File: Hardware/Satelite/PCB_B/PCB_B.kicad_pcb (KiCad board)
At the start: 2 copper layers, 54 x 54 mm, 66 parts, among them IC1 MCP1642B-50I_MS, IC2 MCP1642B-50I_MS, J1 Conector_PCB_B-C, J2 Conector_PCB_A-B, U1 MIC5323-3.3YD5_TR, U2 ADP2108AUJ-3.3, U3 INA194, U4 MCP6001-OT, U5 INA194, U6 MCP6001-OT, U7 INA194, U8 BQ24091DGQT, U9 BQ27441DRZR-G1A

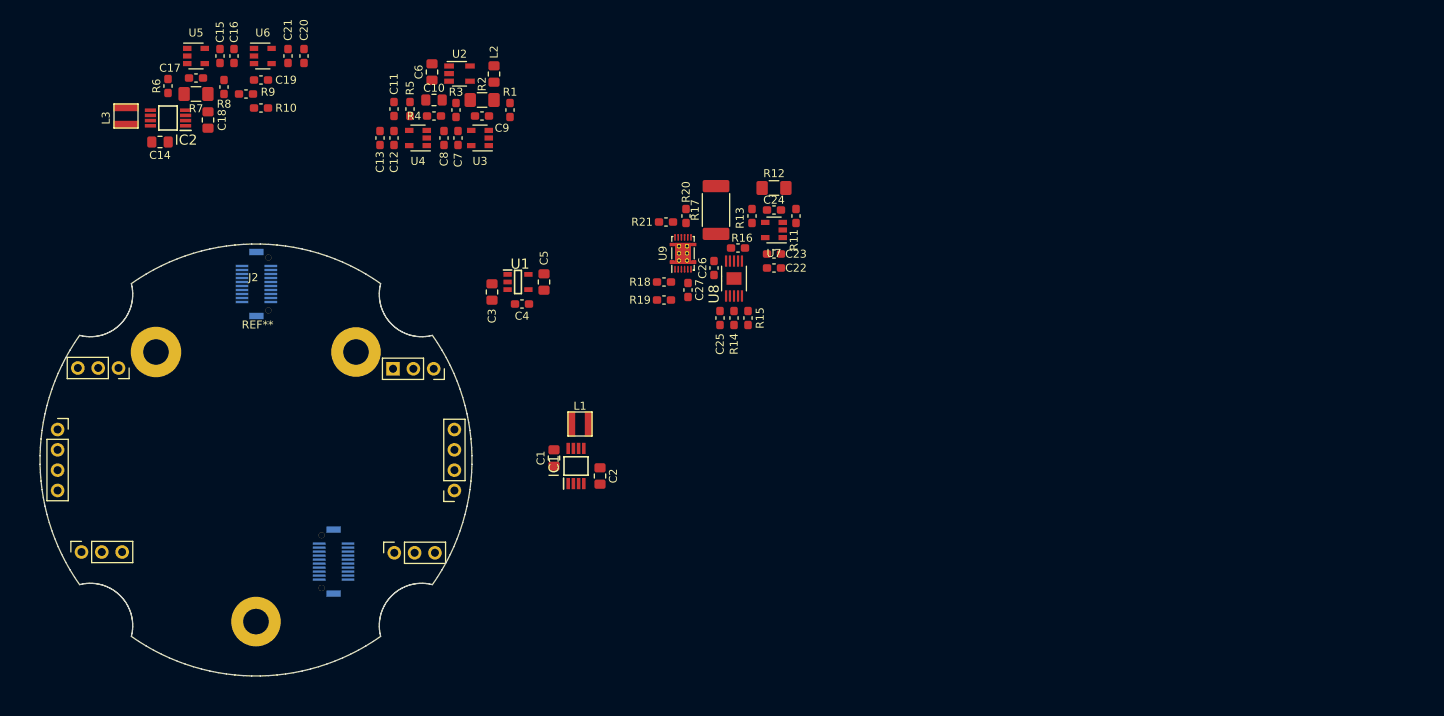
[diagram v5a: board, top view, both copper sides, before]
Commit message: Modifificaciones de pines en conector PCB_B-C
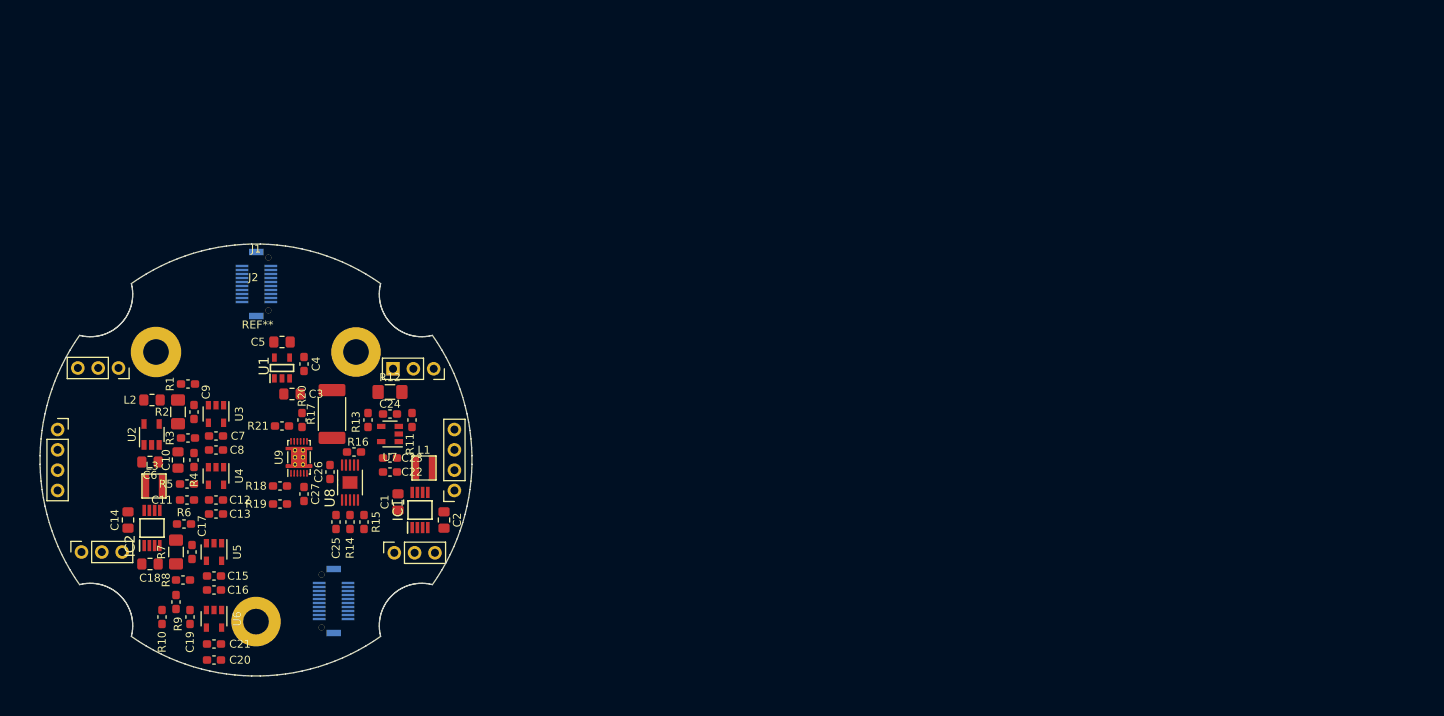
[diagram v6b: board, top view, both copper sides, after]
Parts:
- moved C20 76.3 mm to (-5.25, 25.0), turned to 0 degrees
- moved C21 74.1 mm to (-5.25, 23.0), turned to 0 degrees
- moved U6 70.6 mm to (-5.25, 19.9), turned to 270 degrees
- moved C19 67.7 mm to (-8.25, 19.6), turned to 90 degrees
- moved C16 66.8 mm to (-5.25, 16.2), turned to 0 degrees
- moved C15 65.0 mm to (-5.25, 14.5), turned to 0 degrees
- moved R10 64.8 mm to (-11.8, 19.6), turned to 90 degrees
- moved R9 64.1 mm to (-10.0, 17.8), turned to 90 degrees
- moved U5 62.0 mm to (-5.25, 11.5), turned to 270 degrees
- moved R8 61.8 mm to (-9.12, 15.0), turned to 0 degrees
- moved C6 60.2 mm to (-13.2, 0.25), turned to 180 degrees
- moved U2 59.3 mm to (-13.1, -3.19), turned to 90 degrees
- moved C17 59.3 mm to (-8.00, 11.5), turned to 90 degrees
- moved L2 59.1 mm to (-13.0, -7.50), turned to 0 degrees
- moved R7 57.3 mm to (-10.0, 11.5), turned to 90 degrees
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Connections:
- IC2 pad 1: /Power 5V/CTRL -> /ENABLE_5V
- J1 pad 1: +BATT -> GND
- J1 pad 10: /I_SENSE_3V3 -> +3V3_Internal
- J1 pad 11: /V_SENSE_3V3 -> /V_SENSE_5V
- J1 pad 12: /V_SENSE_5V -> /I_SENSE_5V
- J1 pad 13: GND -> +5V
- J1 pad 14: +5V -> /ENABLE_5V
- J1 pad 15: GND -> /V_SENSE_3V3
- J1 pad 16: GND -> /I_SENSE_3V3
- J1 pad 17: GND -> +3V3
- J1 pad 18: +3V3 -> /ENABLE_3V3
- J1 pad 19: +BATT -> /P1
- J1 pad 2: +BATT -> GND
- J1 pad 20: +BATT -> /GPS_TX
- J1 pad 21: /I_SENSE_BATT -> GND
- J1 pad 22: /GPS_TX -> GND
- J1 pad 23: /P1 -> GND
- J1 pad 24: /SCLK -> /GPOUT
- J1 pad 25: /CS -> /SCL
- J1 pad 26: /SDI -> /SDA
- J1 pad 28: /S_PARACAIDAS -> /CHG_DISABLE
- J1 pad 29: /S_GLOBO -> /CHG
- J1 pad 3: +3V3 -> GND
- J1 pad 30: /GPOUT -> /ISET
- J1 pad 31: /SDA -> /I_SENSE_BATT
- J1 pad 32: /SCL -> /S_GLOBO
- J1 pad 33: /CHG_DISABLE -> /S_PARACAIDAS
- J1 pad 34: /ISET -> /SDO
- J1 pad 35: /CHG -> /SCLK
- J1 pad 36: GND -> /CS
- J1 pad 37: GND -> /SDI
- J1 pad 4: GND -> +3V3
- J1 pad 5: GND -> +5V
- J1 pad 6: GND -> +BATT
- J1 pad 7: +5V -> +BATT
- J1 pad 8: GND -> +BATT
- J1 pad 9: /I_SENSE_5V -> +BATT
- U2 pad 3: /Power 3V3/CTRL -> /ENABLE_3V3

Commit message: PCB_B Terminado sujeto a revision
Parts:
- moved R16 2.15 mm to (10.1, -1.00), turned to 0 degrees
- moved C14 0.25 mm to (-16.0, 7.25)
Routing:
- net GND: track 0.00 -> 154.8 mm, vias 0 -> 25
- net +3V3_Internal: track 0.00 -> 141.0 mm, vias 0 -> 9
- net +BATT: track 0.00 -> 107.9 mm, vias 0 -> 2
- net +5V: track 0.00 -> 49.3 mm, vias 0 -> 1
- net /V_SENSE_5V: track 0.00 -> 43.8 mm, vias 0 -> 1
- net /ENABLE_5V: track 0.00 -> 40.2 mm, vias 0 -> 1
- net +3V3: track 0.00 -> 38.0 mm, vias 0 -> 1
- net /I_SENSE_5V: track 0.00 -> 34.3 mm, vias 0 -> 1
- net /V_SENSE_3V3: track 0.00 -> 32.2 mm, vias 0 -> 1
- net /ENABLE_3V3: track 0.00 -> 28.3 mm, vias 0 -> 1
- net /GPOUT: track 0.00 -> 28.2 mm, vias 0 -> 1
- net /Fuel Gauge/VBAT: track 0.00 -> 27.2 mm, vias 0 -> 4
- net /S_GLOBO: track 0.00 -> 25.8 mm
- net /S_PARACAIDAS: track 0.00 -> 25.4 mm
- net /ISET: track 0.00 -> 25.3 mm, vias 0 -> 1
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- added copper zone on B.Cu, net GND
- added copper zone on F.Cu, net GND

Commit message: Correciones en PCB_B
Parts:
- moved R18 0.67 mm to (2.50, 3.70)
- moved U9 0.66 mm to (4.71, -0.34)
- moved R19 0.64 mm to (2.50, 5.90)
- moved C2 0.42 mm to (23.2, 7.80)
- moved R1 0.41 mm to (-8.10, -9.40)
- moved L1 0.40 mm to (20.6, 1.00)
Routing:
- net GND: track 154.8 -> 179.7 mm, vias 25 -> 26
- net +BATT: track 107.9 -> 122.7 mm, vias 2 -> 3
- net Net-(IC1-Pad5): track 3.37 -> 7.01 mm
- net /SCL: track 19.6 -> 22.7 mm
- net /SDA: track 20.9 -> 18.7 mm
- net /Fuel Gauge/VBAT: track 27.2 -> 28.7 mm
- net /SERVOS_5V: track 17.1 -> 18.0 mm
- net /ISET: track 25.3 -> 24.5 mm
